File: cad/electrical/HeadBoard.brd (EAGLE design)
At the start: 91.4 x 75.9 mm, 10 parts, among them U1 ABX00087

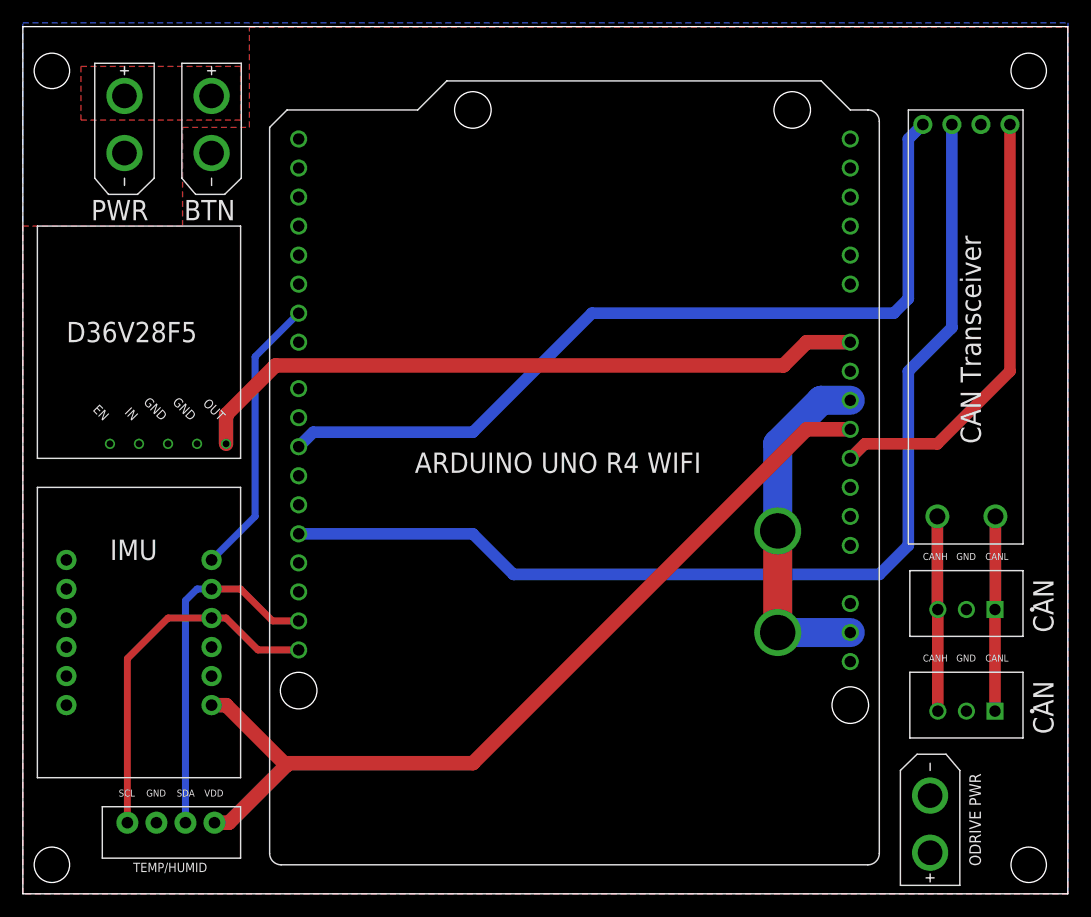
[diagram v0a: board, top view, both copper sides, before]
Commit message: Update pcb component sizes and power connections
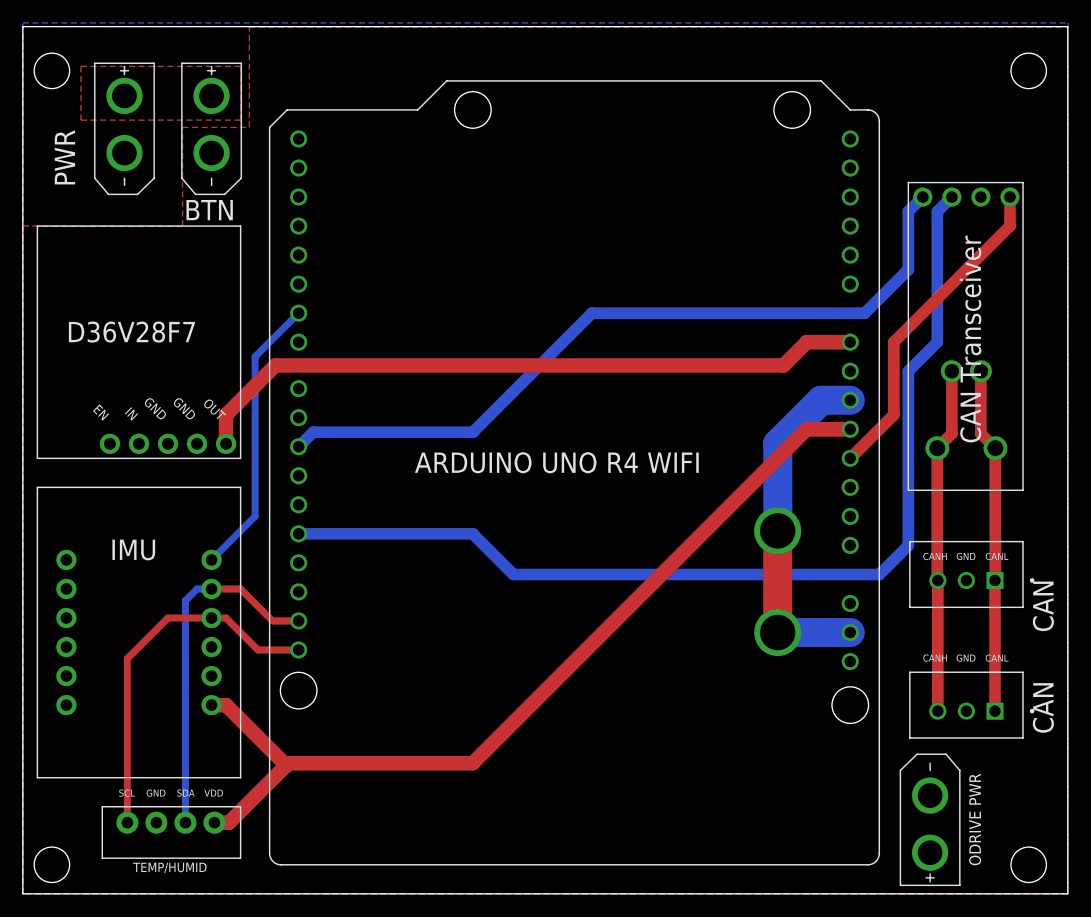
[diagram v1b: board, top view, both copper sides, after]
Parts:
- moved U$2 6.35 mm to (77.5, 62.2)
- moved CAN_CONN 2.54 mm to (82.5, 27.9)
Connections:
- net CANH: now also U$2.CANH@1, U$2.CANH@2; no longer U$2.CANH
- net CANL: now also U$2.CANL@1, U$2.CANL@2; no longer U$2.CANL
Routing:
- net CANL: track 17.1 -> 30.3 mm
- net CANH: track 17.1 -> 30.3 mm
- net 3V3: track 38.7 -> 28.6 mm
- net CANTX: track 74.5 -> 66.6 mm
- net CANRX: track 94.3 -> 87.9 mm
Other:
- board text added: "D36V28F7"
- board text added: "Ribbon Fin Robot Control Board Version 1.01 - 08/16/2024 Iman Adibnazari Bioinspired Robotics and Design Lab UC San Diego"
- board text removed: "D36V28F5"
- board text removed: "Ribbon Fin Robot Control Board Version 1.00 - 08/16/2024 Iman Adibnazari Bioinspired Robotics and Design Lab UC San Diego"
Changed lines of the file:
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@@
 <wire x1="91.42" y1="75.87" x2="0" y2="75.87" width="0" layer="20"/>
 <wire x1="0" y1="75.87" x2="0" y2="0" width="0" layer="20"/>
-<text x="5.969" y="58.928" size="1.778" layer="21">PWR</text>
+<text x="4.572" y="61.849" size="1.778" layer="21" rot="R90">PWR</text>
 <text x="14.097" y="58.928" size="1.778" layer="21">BTN</text>
-<text x="3.81" y="48.26" size="1.778" layer="21">D36V28F5</text>
+<text x="3.81" y="48.26" size="1.778" layer="21">D36V28F7</text>
 <text x="7.62" y="29.21" size="1.778" layer="21">IMU</text>
 <text x="9.652" y="1.905" size="0.8128" layer="21">TEMP/HUMID</text>
@@
 <text x="82.804" y="10.541" size="1.016" layer="21" rot="R270">ODRIVE PWR</text>
 <text x="60.96" y="6.35" size="1.27" layer="22" rot="MR0">Ribbon Fin Robot Control Board
-Version 1.00 - 08/16/2024
+Version 1.01 - 08/16/2024
 Iman Adibnazari
 Bioinspired Robotics and Design Lab
@@
 <attribute name="SNAPEDA_LINK" value="https://www.snapeda.com/parts/XT30UPB-M/AMASS/view-part/?ref=snap" x="-48.26" y="17.78" size="1.778" layer="27" rot="R270" display="off"/>
 </element>
-<element name="CAN_CONN" library="B3B-XH-A_LF__SN_" package="JST_B3B-XH-A(LF)(SN)" value="B3B-XH-A(LF)(SN)" x="82.55" y="25.4" smashed="yes">
-<attribute name="AVAILABILITY" value="In Stock" x="124.46" y="-60.96" size="1.778" layer="27" display="off"/>
-<attribute name="CHECK_PRICES" value="https://www.snapeda.com/parts/B3B-XH-A(LF)(SN)/JST+Sales+America+Inc./view-part/?ref=eda" x="124.46" y="-60.96" size="1.778" layer="27" display="off"/>
-<attribute name="DESCRIPTION" value=" Connector Header Through Hole 3 position 0.098 (2.50mm) " x="124.46" y="-60.96" size="1.778" layer="27" display="off"/>
-<attribute name="MF" value="JST Sales" x="124.46" y="-60.96" size="1.778" layer="27" display="off"/>
-<attribute name="MP" value="B3B-XH-A(LF)(SN)" x="124.46" y="-60.96" size="1.778" layer="27" display="off"/>
-<attribute name="PACKAGE" value="None" x="124.46" y="-60.96" size="1.778" layer="27" display="off"/>
-<attribute name="PRICE" value="None" x="124.46" y="-60.96" size="1.778" layer="27" display="off"/>
-<attribute name="SNAPEDA_LINK" value="https://www.snapeda.com/parts/B3B-XH-A(LF)(SN)/JST+Sales+America+Inc./view-part/?ref=snap" x="124.46" y="-60.96" size="1.778" layer="27" display="off"/>
+<element name="CAN_CONN" library="B3B-XH-A_LF__SN_" package="JST_B3B-XH-A(LF)(SN)" value="B3B-XH-A(LF)(SN)" x="82.55" y="27.94" smashed="yes">
+<attribute name="AVAILABILITY" value="In Stock" x="124.46" y="-58.42" size="1.778" layer="27" display="off"/>
+<attribute name="CHECK_PRICES" value="https://www.snapeda.com/parts/B3B-XH-A(LF)(SN)/JST+Sales+America+Inc./view-part/?ref=eda" x="124.46" y="-58.42" size="1.778" layer="27" display="off"/>
+<attribute name="DESCRIPTION" value=" Connector Header Through Hole 3 position 0.098 (2.50mm) " x="124.46" y="-58.42" size="1.778" layer="27" display="off"/>
+<attribute name="MF" value="JST Sales" x="124.46" y="-58.42" size="1.778" layer="27" display="off"/>
+<attribute name="MP" value="B3B-XH-A(LF)(SN)" x="124.46" y="-58.42" size="1.778" layer="27" display="off"/>
+<attribute name="PACKAGE" value="None" x="124.46" y="-58.42" size="1.778" layer="27" display="off"/>
+<attribute name="PRICE" value="None" x="124.46" y="-58.42" size="1.778" layer="27" display="off"/>
+<attribute name="SNAPEDA_LINK" value="https://www.snapeda.com/parts/B3B-XH-A(LF)(SN)/JST+Sales+America+Inc./view-part/?ref=snap" x="124.46" y="-58.42" size="1.778" layer="27" display="off"/>
 </element>
 <element name="IMU" library="UnderactuatedDorsalFin" package="ADAFRUIT_TDK_INVENSENSE" value="ADAFRUIT_TDK_INVENSENSE" x="10.16" y="22.86" smashed="yes" rot="R90"/>
@@
 <attribute name="STANDARD" value="Manufacturer Recommendations" x="77.47" y="66.04" size="1.778" layer="27" rot="R90" display="off"/>
 </element>
-<element name="U$2" library="UnderactuatedDorsalFin" package="WAVESHARE_SN65HVD230" value="WAVESHARE_SN65HVD230" x="77.47" y="68.58" smashed="yes" rot="R270"/>
+<element name="U$2" library="UnderactuatedDorsalFin" package="WAVESHARE_SN65HVD230" value="WAVESHARE_SN65HVD230" x="77.47" y="62.23" smashed="yes" rot="R270"/>
 <element name="CAN_CONN1" library="B3B-XH-A_LF__SN_" package="JST_B3B-XH-A(LF)(SN)" value="B3B-XH-A(LF)(SN)" x="82.55" y="16.51" smashed="yes">
 <attribute name="AVAILABILITY" value="In Stock" x="82.55" y="16.51" size="1.778" layer="27" display="off"/>
@@
 <wire x1="42.926" y1="27.94" x2="39.37" y2="31.496" width="1.016" layer="16"/>
 <wire x1="74.93" y1="27.94" x2="77.47" y2="30.48" width="1.016" layer="16"/>
-<wire x1="77.47" y1="45.72" x2="81.28" y2="49.53" width="1.016" layer="16"/>
-<wire x1="81.28" y1="67.31" x2="81.28" y2="49.53" width="1.016" layer="16"/>
+<wire x1="77.47" y1="45.72" x2="80.01" y2="48.26" width="1.016" layer="16"/>
+<wire x1="81.28" y1="60.96" x2="80.01" y2="59.69" width="1.016" layer="16"/>
+<wire x1="80.01" y1="59.69" x2="80.01" y2="48.26" width="1.016" layer="16"/>
 <wire x1="77.47" y1="30.48" x2="77.47" y2="45.72" width="1.016" layer="16"/>
 </signal>
@@
 <wire x1="39.37" y1="40.386" x2="25.4" y2="40.386" width="1.016" layer="16"/>
 <wire x1="24.13" y1="39.116" x2="25.4" y2="40.386" width="1.016" layer="16"/>
-<wire x1="49.784" y1="50.8" x2="76.2" y2="50.8" width="1.016" layer="16"/>
-<wire x1="76.2" y1="50.8" x2="77.47" y2="52.07" width="1.016" layer="16"/>
-<wire x1="77.47" y1="66.04" x2="78.74" y2="67.31" width="1.016" layer="16"/>
-<wire x1="77.47" y1="66.04" x2="77.47" y2="52.07" width="1.016" layer="16"/>
+<wire x1="49.784" y1="50.8" x2="73.66" y2="50.8" width="1.016" layer="16"/>
+<wire x1="73.66" y1="50.8" x2="77.47" y2="54.61" width="1.016" layer="16"/>
+<wire x1="77.47" y1="59.69" x2="78.74" y2="60.96" width="1.016" layer="16"/>
+<wire x1="77.47" y1="59.69" x2="77.47" y2="54.61" width="1.016" layer="16"/>
 </signal>
 <signal name="IMU_INT">
@@
 <contactref element="U1" pad="JA4"/>
 <contactref element="U$2" pad="3.3V"/>
-<wire x1="72.39" y1="38.1" x2="73.66" y2="39.37" width="1.016" layer="1"/>
-<wire x1="73.66" y1="39.37" x2="80.01" y2="39.37" width="1.016" layer="1"/>
-<wire x1="80.01" y1="39.37" x2="86.36" y2="45.72" width="1.016" layer="1"/>
-<wire x1="86.36" y1="45.72" x2="86.36" y2="67.31" width="1.016" layer="1"/>
+<wire x1="72.39" y1="38.1" x2="76.2" y2="41.91" width="1.016" layer="1"/>
+<wire x1="86.36" y1="60.96" x2="86.36" y2="58.42" width="1.016" layer="1"/>
+<wire x1="86.36" y1="58.42" x2="76.2" y2="48.26" width="1.016" layer="1"/>
+<wire x1="76.2" y1="48.26" x2="76.2" y2="41.91" width="1.016" layer="1"/>
 </signal>
 <signal name="CANL">
 <contactref element="CAN_CONN" pad="1"/>
-<contactref element="U$2" pad="CANL"/>
-<wire x1="85.09" y1="33.02" x2="85.09" y2="24.915" width="1.016" layer="1"/>
-<wire x1="85.09" y1="24.915" x2="85.05" y2="24.875" width="1.016" layer="1"/>
+<contactref element="U$2" pad="CANL@1"/>
+<wire x1="85.09" y1="38.989" x2="85.09" y2="27.455" width="1.016" layer="1"/>
+<wire x1="85.09" y1="27.455" x2="85.05" y2="27.415" width="1.016" layer="1"/>
 <contactref element="CAN_CONN1" pad="1"/>
-<wire x1="85.05" y1="24.875" x2="85.05" y2="15.985" width="1.016" layer="1"/>
+<wire x1="85.05" y1="27.415" x2="85.05" y2="15.985" width="1.016" layer="1"/>
+<contactref element="U$2" pad="CANL@2"/>
+<wire x1="85.09" y1="38.989" x2="83.82" y2="40.259" width="1.016" layer="1"/>
+<wire x1="83.82" y1="40.259" x2="83.82" y2="45.72" width="1.016" layer="1"/>
 </signal>
 <signal name="CANH">
 <contactref element="CAN_CONN" pad="3"/>
-<contactref element="U$2" pad="CANH"/>
-<wire x1="80.01" y1="33.02" x2="80.01" y2="24.915" width="1.016" layer="1"/>
-<wire x1="80.01" y1="24.915" x2="80.05" y2="24.875" width="1.016" layer="1"/>
+<contactref element="U$2" pad="CANH@1"/>
+<wire x1="80.01" y1="38.989" x2="80.01" y2="27.455" width="1.016" layer="1"/>
+<wire x1="80.05" y1="27.415" x2="80.01" y2="27.455" width="1.016" layer="1"/>
 <contactref element="CAN_CONN1" pad="3"/>
-<wire x1="80.05" y1="24.875" x2="80.05" y2="15.985" width="1.016" layer="1"/>
+<wire x1="80.05" y1="27.415" x2="80.05" y2="15.985" width="1.016" layer="1"/>
+<contactref element="U$2" pad="CANH@2"/>
+<wire x1="80.01" y1="38.989" x2="81.28" y2="40.259" width="1.016" layer="1"/>
+<wire x1="81.28" y1="40.259" x2="81.28" y2="45.72" width="1.016" layer="1"/>
 </signal>
 </signals>
